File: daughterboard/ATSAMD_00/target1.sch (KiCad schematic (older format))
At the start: 20 parts, among them U1 ATSAMD09D14A-M

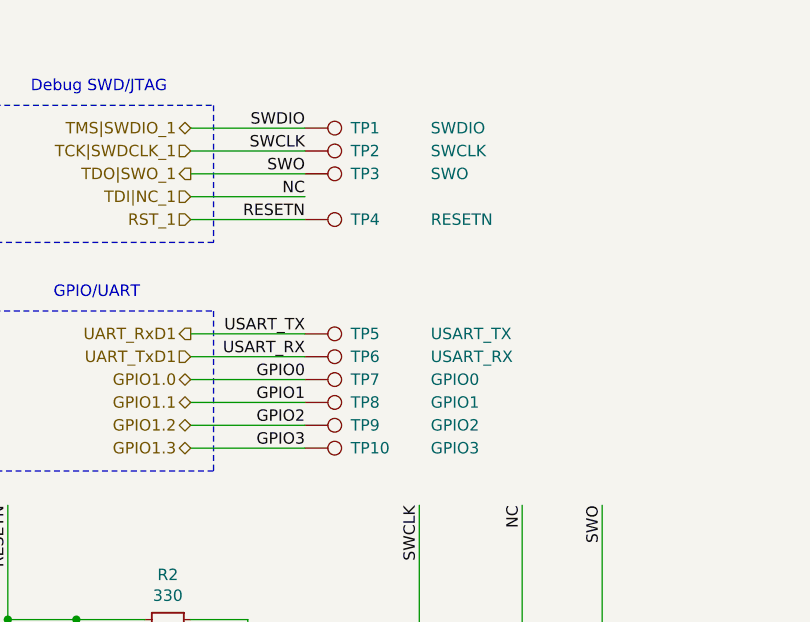
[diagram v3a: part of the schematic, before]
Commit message: finished ATSAMD daughterboard layout
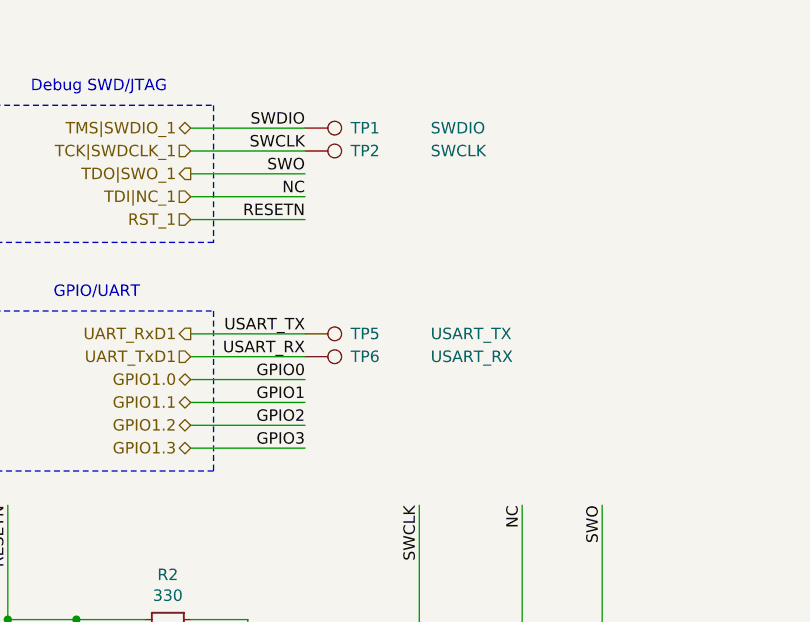
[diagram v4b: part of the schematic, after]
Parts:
- removed TP10: GPIO3, symbol Connector:TestPoint
- removed TP3: SWO, symbol Connector:TestPoint
- removed TP4: RESETN, symbol Connector:TestPoint
- removed TP7: GPIO0, symbol Connector:TestPoint
- removed TP8: GPIO1, symbol Connector:TestPoint
- removed TP9: GPIO2, symbol Connector:TestPoint
- C1, C2, C3: footprint (none) -> Capacitor_SMD:C_0603_1608Metric_Pad1.05x0.95mm_HandSolder
- JP1: footprint (none) -> Jumper:SolderJumper-2_P1.3mm_Open_TrianglePad1.0x1.5mm
- R1, R2, R3, R4, R5: footprint (none) -> Resistor_SMD:R_0603_1608Metric_Pad1.05x0.95mm_HandSolder
- TP1, TP2, TP5, TP6: footprint (none) -> TestPoint:TestPoint_Pad_1.0x1.0mm
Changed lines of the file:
@@
 F 0 "C2" H 7492 1796 50  0000 L CNN
 F 1 "4.7u" H 7492 1705 50  0000 L CNN
-F 2 "" H 7400 1750 50  0001 C CNN
+F 2 "Capacitor_SMD:C_0603_1608Metric_Pad1.05x0.95mm_HandSolder" H 7400 1750 50  0001 C CNN
 F 3 "~" H 7400 1750 50  0001 C CNN
 	1    7400 1750
@@
 F 0 "C3" H 7892 1796 50  0000 L CNN
 F 1 "100n" H 7892 1705 50  0000 L CNN
-F 2 "" H 7800 1750 50  0001 C CNN
+F 2 "Capacitor_SMD:C_0603_1608Metric_Pad1.05x0.95mm_HandSolder" H 7800 1750 50  0001 C CNN
 F 3 "~" H 7800 1750 50  0001 C CNN
 	1    7800 1750
@@
 F 0 "R1" H 859 4346 50  0000 L CNN
 F 1 "10k" H 859 4255 50  0000 L CNN
-F 2 "" H 800 4300 50  0001 C CNN
+F 2 "Resistor_SMD:R_0603_1608Metric_Pad1.05x0.95mm_HandSolder" H 800 4300 50  0001 C CNN
 F 3 "~" H 800 4300 50  0001 C CNN
 	1    800  4300
@@
 F 0 "R2" V 1304 3850 50  0000 C CNN
 F 1 "330" V 1395 3850 50  0000 C CNN
-F 2 "" H 1500 3850 50  0001 C CNN
+F 2 "Resistor_SMD:R_0603_1608Metric_Pad1.05x0.95mm_HandSolder" H 1500 3850 50  0001 C CNN
 F 3 "~" H 1500 3850 50  0001 C CNN
 	1    1500 3850
@@
 F 0 "C1" H 1192 4346 50  0000 L CNN
 F 1 "100n" H 1192 4255 50  0000 L CNN
-F 2 "" H 1100 4300 50  0001 C CNN
+F 2 "Capacitor_SMD:C_0603_1608Metric_Pad1.05x0.95mm_HandSolder" H 1100 4300 50  0001 C CNN
 F 3 "~" H 1100 4300 50  0001 C CNN
 	1    1100 4300
@@
 F 0 "JP1" V 1896 4212 50  0000 R CNN
 F 1 "NRST" V 1805 4212 50  0000 R CNN
-F 2 "" H 1850 4300 50  0001 C CNN
+F 2 "Jumper:SolderJumper-2_P1.3mm_Open_TrianglePad1.0x1.5mm" H 1850 4300 50  0001 C CNN
 F 3 "~" H 1850 4300 50  0001 C CNN
 	1    1850 4300
@@
 F 0 "R3" H 2659 4296 50  0000 L CNN
 F 1 "1k" H 2659 4205 50  0000 L CNN
-F 2 "" H 2600 4250 50  0001 C CNN
+F 2 "Resistor_SMD:R_0603_1608Metric_Pad1.05x0.95mm_HandSolder" H 2600 4250 50  0001 C CNN
 F 3 "~" H 2600 4250 50  0001 C CNN
 	1    2600 4250
@@
 F 0 "R4" H 3109 4296 50  0000 L CNN
 F 1 "100k" H 3109 4205 50  0000 L CNN
-F 2 "" H 3050 4250 50  0001 C CNN
+F 2 "Resistor_SMD:R_0603_1608Metric_Pad1.05x0.95mm_HandSolder" H 3050 4250 50  0001 C CNN
 F 3 "~" H 3050 4250 50  0001 C CNN
 	1    3050 4250
@@
 F 0 "R5" H 3459 4296 50  0000 L CNN
 F 1 "100k" H 3459 4205 50  0000 L CNN
-F 2 "" H 3400 4250 50  0001 C CNN
+F 2 "Resistor_SMD:R_0603_1608Metric_Pad1.05x0.95mm_HandSolder" H 3400 4250 50  0001 C CNN
 F 3 "~" H 3400 4250 50  0001 C CNN
 	1    3400 4250
@@
 F 0 "TP1" V 2100 1900 50  0000 L CNN
 F 1 "SWDIO" V 2100 2250 50  0000 L CNN
-F 2 "" H 2300 1700 50  0001 C CNN
+F 2 "TestPoint:TestPoint_Pad_1.0x1.0mm" H 2300 1700 50  0001 C CNN
 F 3 "~" H 2300 1700 50  0001 C CNN
 	1    2100 1700
@@
 F 0 "TP2" V 2100 2000 50  0000 L CNN
 F 1 "SWCLK" V 2100 2350 50  0000 L CNN
-F 2 "" H 2300 1800 50  0001 C CNN
+F 2 "TestPoint:TestPoint_Pad_1.0x1.0mm" H 2300 1800 50  0001 C CNN
 F 3 "~" H 2300 1800 50  0001 C CNN
 	1    2100 1800
-	0    1    1    0
-$EndComp
-$Comp
-L Connector:TestPoint TP?
-U 1 1 619256C7
-P 2100 1900
-AR Path="/616688D6/619256C7" Ref="TP?"  Part="1"
-AR Path="/61667F91/619256C7" Ref="TP3"  Part="1"
-F 0 "TP3" V 2100 2100 50  0000 L CNN
-F 1 "SWO" V 2100 2450 50  0000 L CNN
-F 2 "" H 2300 1900 50  0001 C CNN
-F 3 "~" H 2300 1900 50  0001 C CNN
-	1    2100 1900
-	0    1    1    0
-$EndComp
-$Comp
-L Connector:TestPoint TP?
-U 1 1 619256CD
-P 2100 2100
-AR Path="/616688D6/619256CD" Ref="TP?"  Part="1"
-AR Path="/61667F91/619256CD" Ref="TP4"  Part="1"
-F 0 "TP4" V 2100 2300 50  0000 L CNN
-F 1 "RESETN" V 2100 2650 50  0000 L CNN
-F 2 "" H 2300 2100 50  0001 C CNN
-F 3 "~" H 2300 2100 50  0001 C CNN
-	1    2100 2100
 	0    1    1    0
 $EndComp
@@
 F 0 "TP5" V 2100 2800 50  0000 L CNN
 F 1 "USART_TX" V 2100 3150 50  0000 L CNN
-F 2 "" H 2300 2600 50  0001 C CNN
+F 2 "TestPoint:TestPoint_Pad_1.0x1.0mm" H 2300 2600 50  0001 C CNN
 F 3 "~" H 2300 2600 50  0001 C CNN
 	1    2100 2600
@@
 F 0 "TP6" V 2100 2900 50  0000 L CNN
 F 1 "USART_RX" V 2100 3250 50  0000 L CNN
-F 2 "" H 2300 2700 50  0001 C CNN
+F 2 "TestPoint:TestPoint_Pad_1.0x1.0mm" H 2300 2700 50  0001 C CNN
 F 3 "~" H 2300 2700 50  0001 C CNN
 	1    2100 2700
 	0    1    -1   0
 $EndComp
-$Comp
-L Connector:TestPoint TP?
-U 1 1 619256DF
-P 2100 2800
-AR Path="/616688D6/619256DF" Ref="TP?"  Part="1"
-AR Path="/61667F91/619256DF" Ref="TP7"  Part="1"
-F 0 "TP7" V 2100 3000 50  0000 L CNN
-F 1 "GPIO0" V 2100 3350 50  0000 L CNN
-F 2 "" H 2300 2800 50  0001 C CNN
-F 3 "~" H 2300 2800 50  0001 C CNN
-	1    2100 2800
-	0    1    -1   0
-$EndComp
-$Comp
-L Connector:TestPoint TP?
-U 1 1 619256E5
-P 2100 2900
-AR Path="/616688D6/619256E5" Ref="TP?"  Part="1"
-AR Path="/61667F91/619256E5" Ref="TP8"  Part="1"
-F 0 "TP8" V 2100 3100 50  0000 L CNN
-F 1 "GPIO1" V 2100 3450 50  0000 L CNN
-F 2 "" H 2300 2900 50  0001 C CNN
-F 3 "~" H 2300 2900 50  0001 C CNN
-	1    2100 2900
-	0    1    -1   0
-$EndComp
-$Comp
-L Connector:TestPoint TP?
-U 1 1 619256EB
-P 2100 3000
-AR Path="/616688D6/619256EB" Ref="TP?"  Part="1"
-AR Path="/61667F91/619256EB" Ref="TP9"  Part="1"
-F 0 "TP9" V 2100 3200 50  0000 L CNN
-F 1 "GPIO2" V 2100 3550 50  0000 L CNN
-F 2 "" H 2300 3000 50  0001 C CNN
-F 3 "~" H 2300 3000 50  0001 C CNN
-	1    2100 3000
-	0    1    -1   0
-$EndComp
-$Comp
-L Connector:TestPoint TP?
-U 1 1 619256F1
-P 2100 3100
-AR Path="/616688D6/619256F1" Ref="TP?"  Part="1"
-AR Path="/61667F91/619256F1" Ref="TP10"  Part="1"
-F 0 "TP10" V 2100 3300 50  0000 L CNN
-F 1 "GPIO3" V 2100 3650 50  0000 L CNN
-F 2 "" H 2300 3100 50  0001 C CNN
-F 3 "~" H 2300 3100 50  0001 C CNN
-	1    2100 3100
-	0    1    -1   0
-$EndComp
